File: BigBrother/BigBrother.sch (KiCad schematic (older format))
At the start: 4 parts

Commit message: BigBrother Update
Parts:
- gave numbers to parts that had none: 2
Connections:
- net 3.3V: now reaches J?.1 (3.3V)
- net 3.3V: now also J?.17 (3.3V), U1.1 (VIN), U1.9 (PS1), U2.1 (Vin)
- net RXD: now reaches J?.10 (GPIO15_RXD0)
- net RXD: now also U1.4 (SDA)
- net GPIO_INA: now reaches J?.11 (GPIO17)
- net GPIO_INA: now also U?.4 (INA)
- net GPIO_INB: now reaches J?.13 (GPIO27)
- net GPIO_INB: now also U?.10 (INB)
- net GND: now reaches J?.25 (GND)
- net GND: now also J?.9 (GND), U1.3 (GND), U2.3 (GND)
- net SDA: now reaches J?.3 (GPIO02_SDA1_I2C)
- net SDA: now also U2.6 (SDI)
- net GPIO_PWM: now reaches J?.33 (GPIO13)
- net GPIO_PWM: now also U?.7 (PWM)
- net SCL: now reaches J?.5 (GPIO03_SCL1_I2C)
- net SCL: now also U2.4 (SCK)
- net TXD: now reaches J?.8 (GPIO14_TXD0)
- net TXD: now also U1.5 (SCL)
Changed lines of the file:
@@
 $EndComp
 $Comp
-L bno055-breakout:bno055 U?
+L BMP388:BMP388 U2
+U 1 1 5E48BA81
+P 8300 5000
+F 0 "U2" H 8778 5046 50  0000 L CNN
+F 1 "BMP388" H 8778 4955 50  0000 L CNN
+F 2 "MODULE" H 8300 5000 50  0001 C CNN
+F 3 "DOCUMENTATION" H 8300 5000 50  0001 C CNN
+	1    8300 5000
+	1    0    0    -1
+$EndComp
+Text GLabel 1550 1350 0    50   Input ~ 0
+3.3V
+Text GLabel 1550 1750 0    50   Input ~ 0
+GND
+Text GLabel 3450 1750 2    50   Input ~ 0
+RXD
+Text GLabel 7800 2500 0    50   Input ~ 0
+GND
+Text GLabel 7800 2200 0    50   Input ~ 0
+3.3V
+$Comp
+L bno055-breakout:bno055 U1
 U 1 1 5E48AFB4
 P 7900 2100
-F 0 "U?" H 8300 2265 50  0000 C CNN
+F 0 "U1" H 8300 2265 50  0000 C CNN
 F 1 "bno055" H 8300 2174 50  0000 C CNN
 F 2 "" H 8250 2250 50  0001 C CNN
@@
 	1    0    0    -1
 $EndComp
-$Comp
-L BMP388:BMP388 U?
-U 1 1 5E48BA81
-P 8300 5000
-F 0 "U?" H 8778 5046 50  0000 L CNN
-F 1 "BMP388" H 8778 4955 50  0000 L CNN
-F 2 "MODULE" H 8300 5000 50  0001 C CNN
-F 3 "DOCUMENTATION" H 8300 5000 50  0001 C CNN
-	1    8300 5000
-	1    0    0    -1
-$EndComp
+Text GLabel 7800 2650 0    50   Input ~ 0
+RXD
+Text GLabel 3450 1650 2    50   Input ~ 0
+TXD
+Text GLabel 7800 2800 0    50   Input ~ 0
+TXD
+Text GLabel 8800 2500 2    50   Input ~ 0
+3.3V
+Text GLabel 1550 2150 0    50   Input ~ 0
+3.3V
+Text GLabel 7550 4650 0    50   Input ~ 0
+3.3V
+Text GLabel 1550 2550 0    50   Input ~ 0
+GND
+Text GLabel 7550 4850 0    50   Input ~ 0
+GND
+Text GLabel 1550 1550 0    50   Input ~ 0
+SCL
+Text GLabel 7550 4950 0    50   Input ~ 0
+SCL
+Text GLabel 1550 1450 0    50   Input ~ 0
+SDA
+Text GLabel 7550 5150 0    50   Input ~ 0
+SDA
+Text GLabel 1550 2950 0    50   Input ~ 0
+GPIO_PWM
+Text GLabel 1950 5700 0    50   Input ~ 0
+GPIO_PWM
+Text GLabel 1550 1850 0    50   Input ~ 0
+GPIO_INA
+Text GLabel 1950 5500 0    50   Input ~ 0
+GPIO_INA
+Text GLabel 1550 1950 0    50   Input ~ 0
+GPIO_INB
+Text GLabel 1950 5600 0    50   Input ~ 0
+GPIO_INB
 $EndSCHEMATC

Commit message: Board updates
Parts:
- removed U?: VNH5019A-E, Package_SO:ST_MultiPowerSO-30, symbol Driver_Motor:VNH5019A-E
- added U3: VHN5019_Breakout, symbol NUSTARS:VHN5019_Breakout
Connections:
- net 3.3V: now also U3.7 (VDD)
- net GND: now also U3.8 (GND); no longer J?.25 (GND)
- net GPIO_INA: now also U3.1 (INA)
- net GPIO_INB: now also U3.6 (INB)
- net GPIO_PWM: now also U3.3 (PWM)
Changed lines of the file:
@@
-$EndComp
-$Comp
-L Driver_Motor:VNH5019A-E U?
-U 1 1 5E48A221
-P 2450 5900
-F 0 "U?" H 2450 6681 50  0000 C CNN
-F 1 "VNH5019A-E" H 2450 6590 50  0000 C CNN
-F 2 "Package_SO:ST_MultiPowerSO-30" H 3350 5350 50  0001 C CNN
-F 3 "https://www.st.com/resource/en/datasheet/vnh5019a-e.pdf" H 2000 6750 50  0001 C CNN
-	1    2450 5900
-	1    0    0    -1
 $EndComp
 $Comp
@@
 Text GLabel 7550 4650 0    50   Input ~ 0
 3.3V
-Text GLabel 1550 2550 0    50   Input ~ 0
-GND
 Text GLabel 7550 4850 0    50   Input ~ 0
 GND
@@
 Text GLabel 1550 2950 0    50   Input ~ 0
 GPIO_PWM
-Text GLabel 1950 5700 0    50   Input ~ 0
-GPIO_PWM
 Text GLabel 1550 1850 0    50   Input ~ 0
-GPIO_INA
-Text GLabel 1950 5500 0    50   Input ~ 0
 GPIO_INA
 Text GLabel 1550 1950 0    50   Input ~ 0
 GPIO_INB
-Text GLabel 1950 5600 0    50   Input ~ 0
+$Comp
+L NUSTARS:VHN5019_Breakout U3
+U 1 1 5E4A476C
+P 2100 5100
+F 0 "U3" H 2475 5275 50  0000 C CNN
+F 1 "VHN5019_Breakout" H 2475 5184 50  0000 C CNN
+F 2 "" H 2900 5200 50  0001 C CNN
+F 3 "" H 2900 5200 50  0001 C CNN
+	1    2100 5100
+	1    0    0    -1
+$EndComp
+Text GLabel 2000 5150 0    50   Input ~ 0
+GPIO_INA
+Text GLabel 2000 5650 0    50   Input ~ 0
 GPIO_INB
+Text GLabel 2000 5350 0    50   Input ~ 0
+GPIO_PWM
+Text GLabel 2000 5850 0    50   Input ~ 0
+GND
+Text GLabel 2000 5750 0    50   Input ~ 0
+3.3V
 $EndSCHEMATC

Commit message: Boarddddd
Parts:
- J1: renamed from J?; footprint (none) -> Raspberry Pi Zero:RPI_Zero
- U1: footprint (none) -> NUSTARS:bno055
- U2: footprint MODULE -> BMP388:BMP388
- U3: footprint (none) -> NUSTARS:VNH5019_breakout
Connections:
- net 3.3V: no longer J1.1 (3.3V)
- net GND: now also J1.20 (GND)
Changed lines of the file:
@@
 EESchema Schematic File Version 4
+LIBS:BigBrother-cache
 EELAYER 30 0
 EELAYER END
@@
 $EndDescr
 $Comp
-L Connector-ML:RPi_GPIO J?
-U 1 1 5E488C88
-P 1750 1350
-F 0 "J?" H 2500 1637 60  0000 C CNN
-F 1 "RPi_GPIO" H 2500 1531 60  0000 C CNN
-F 2 "" H 1750 1350 60  0000 C CNN
-F 3 "" H 1750 1350 60  0000 C CNN
-	1    1750 1350
-	1    0    0    -1
-$EndComp
-$Comp
 L BMP388:BMP388 U2
 U 1 1 5E48BA81
@@
 F 0 "U2" H 8778 5046 50  0000 L CNN
 F 1 "BMP388" H 8778 4955 50  0000 L CNN
-F 2 "MODULE" H 8300 5000 50  0001 C CNN
+F 2 "BMP388:BMP388" H 8300 5000 50  0001 C CNN
 F 3 "DOCUMENTATION" H 8300 5000 50  0001 C CNN
 	1    8300 5000
 	1    0    0    -1
 $EndComp
-Text GLabel 1550 1350 0    50   Input ~ 0
-3.3V
 Text GLabel 1550 1750 0    50   Input ~ 0
 GND
@@
 F 0 "U1" H 8300 2265 50  0000 C CNN
 F 1 "bno055" H 8300 2174 50  0000 C CNN
-F 2 "" H 8250 2250 50  0001 C CNN
+F 2 "NUSTARS:bno055" H 8250 2250 50  0001 C CNN
 F 3 "" H 8250 2250 50  0001 C CNN
 	1    7900 2100
@@
 F 0 "U3" H 2475 5275 50  0000 C CNN
 F 1 "VHN5019_Breakout" H 2475 5184 50  0000 C CNN
-F 2 "" H 2900 5200 50  0001 C CNN
+F 2 "NUSTARS:VNH5019_breakout" H 2900 5200 50  0001 C CNN
 F 3 "" H 2900 5200 50  0001 C CNN
 	1    2100 5100
@@
 Text GLabel 2000 5750 0    50   Input ~ 0
 3.3V
+$Comp
+L Connector-ML:RPi_GPIO J1
+U 1 1 5E488C88
+P 1750 1350
+F 0 "J1" H 2500 1637 60  0000 C CNN
+F 1 "RPi_GPIO" H 2500 1531 60  0000 C CNN
+F 2 "Raspberry Pi Zero:RPI_Zero" H 1750 1350 60  0001 C CNN
+F 3 "" H 1750 1350 60  0000 C CNN
+	1    1750 1350
+	1    0    0    -1
+$EndComp
+Text GLabel 3450 2250 2    50   Input ~ 0
+GND
 $EndSCHEMATC

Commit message: Board!! maybe done!!!
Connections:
- net 3.3V: now also J1.1 (3.3V)
- net GND: now also J1.14 (GND), J1.25 (GND), J1.30 (GND), J1.34 (GND), J1.39 (GND), J1.6 (GND)
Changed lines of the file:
@@
 Text GLabel 3450 2250 2    50   Input ~ 0
 GND
+Text GLabel 1550 1350 0    50   Input ~ 0
+3.3V
+Text GLabel 1550 2550 0    50   Input ~ 0
+GND
+Text GLabel 1550 3250 0    50   Input ~ 0
+GND
+Text GLabel 3450 1550 2    50   Input ~ 0
+GND
+Text GLabel 3450 1950 2    50   Input ~ 0
+GND
+Text GLabel 3450 2750 2    50   Input ~ 0
+GND
+Text GLabel 3450 2950 2    50   Input ~ 0
+GND
 $EndSCHEMATC

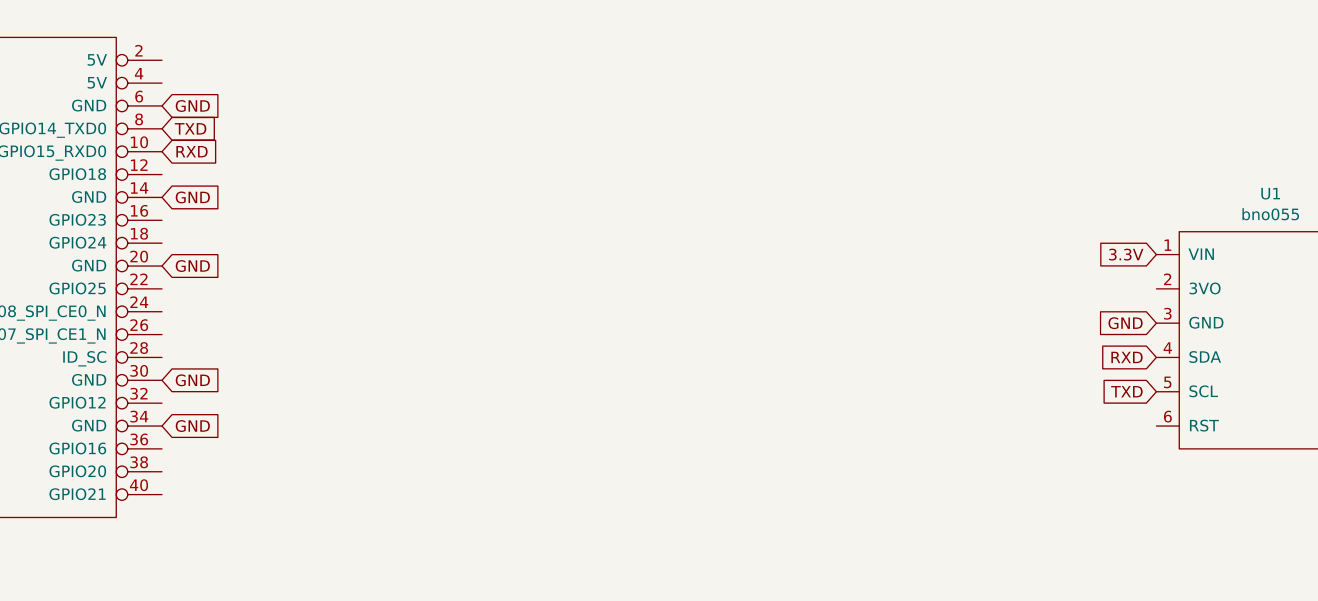
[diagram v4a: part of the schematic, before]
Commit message: I forgot RST
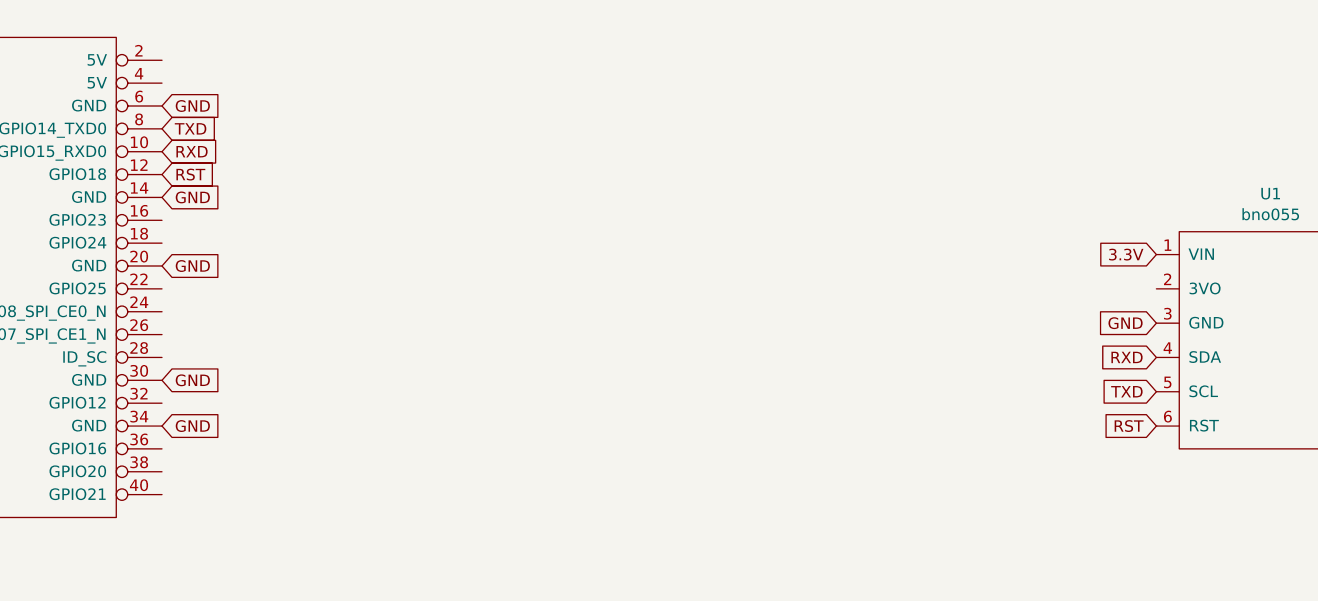
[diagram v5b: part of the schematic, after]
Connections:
- net RST: now reaches J1.12 (GPIO18)
- net RST: now also U1.6 (RST)
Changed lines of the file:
@@
 Text GLabel 3450 2950 2    50   Input ~ 0
 GND
+Text GLabel 7800 2950 0    50   Input ~ 0
+RST
+Text GLabel 3450 1850 2    50   Input ~ 0
+RST
 $EndSCHEMATC
